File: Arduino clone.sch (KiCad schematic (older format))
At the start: 13 parts, among them U1 24LC1025, U2 24LC1025, U3 DS1337_AM, U4 ATMEGA328P-AU, Y1 Crystal, Y2 Crystal

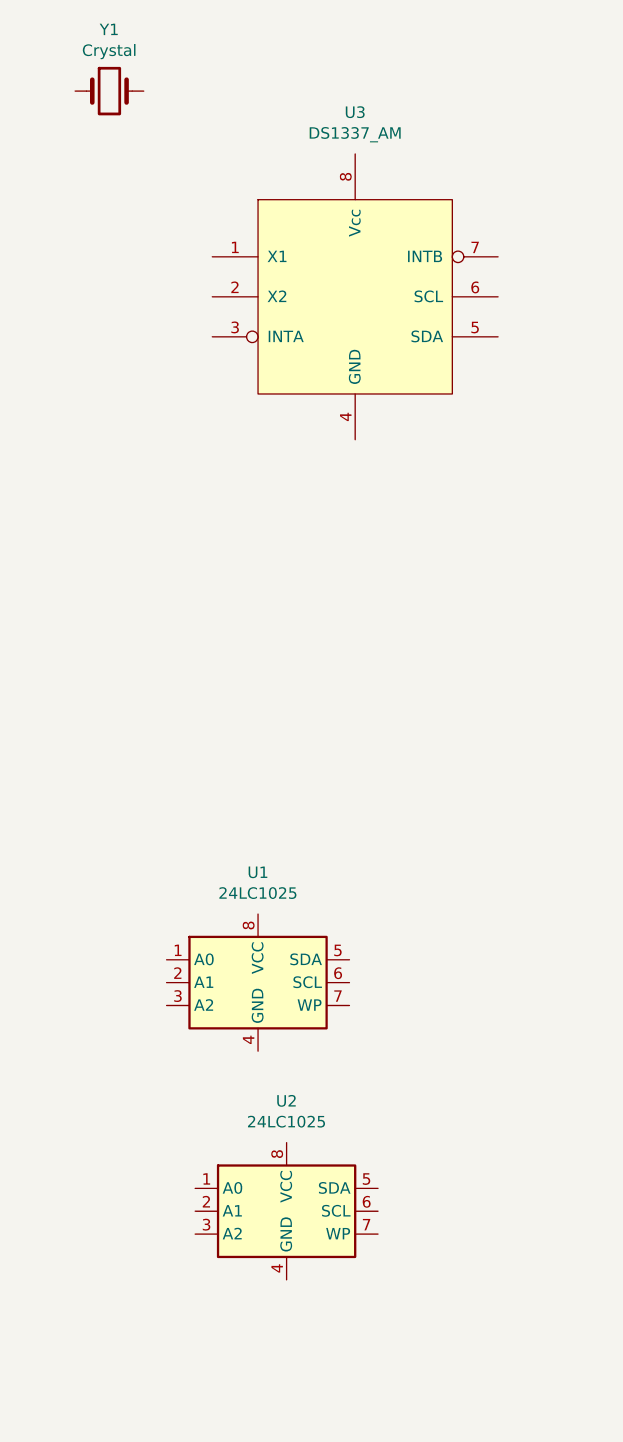
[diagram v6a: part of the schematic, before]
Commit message: Assigned footprints to symbols
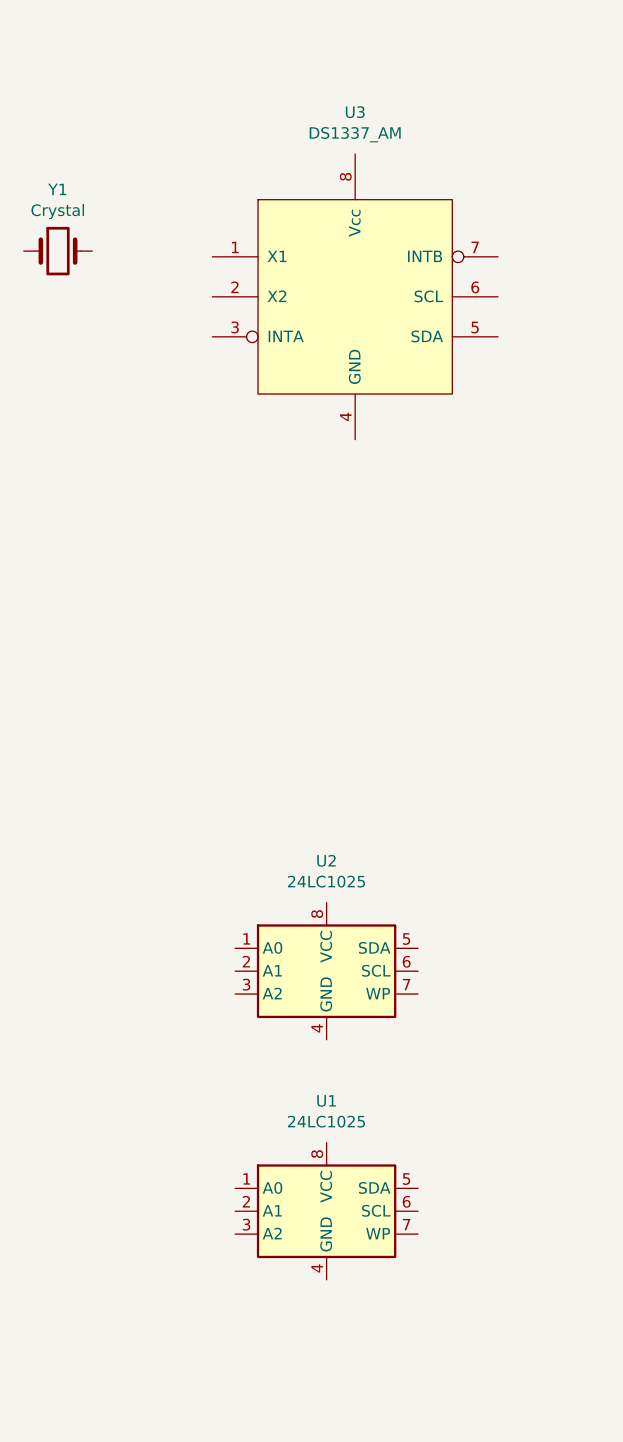
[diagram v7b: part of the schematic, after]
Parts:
- BT1: footprint (none) -> Connector_PinHeader_2.54mm:PinHeader_1x02_P2.54mm_Vertical
- C1, C2, C3: footprint (none) -> Capacitor_SMD:C_0805_2012Metric_Pad1.18x1.45mm_HandSolder
- D1: footprint (none) -> LED_SMD:LED_0805_2012Metric_Pad1.15x1.40mm_HandSolder
- R1, R2: footprint (none) -> Resistor_SMD:R_0805_2012Metric_Pad1.20x1.40mm_HandSolder
- U1, U2: footprint (none) -> Package_SO:SOIJ-8_5.3x5.3mm_P1.27mm
- U3: footprint (none) -> Package_SO:SO-8_5.3x6.2mm_P1.27mm
- Y1: footprint (none) -> Crystal:Crystal_SMD_MicroCrystal_CC7V-T1A-2Pin_3.2x1.5mm_HandSoldering
- Y2: footprint (none) -> Crystal:Crystal_SMD_5032-2Pin_5.0x3.2mm_HandSoldering
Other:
- moved on the sheet: U1, U2, Y1
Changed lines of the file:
@@
 F 0 "BT1" H 9558 1546 50  0000 L CNN
 F 1 "Battery" H 9558 1455 50  0000 L CNN
-F 2 "" V 9450 1560 50  0001 C CNN
+F 2 "Connector_PinHeader_2.54mm:PinHeader_1x02_P2.54mm_Vertical" V 9450 1560 50  0001 C CNN
 F 3 "~" V 9450 1560 50  0001 C CNN
 	1    9450 1500
@@
 F 0 "C1" H 4815 2546 50  0000 L CNN
 F 1 "C" H 4815 2455 50  0000 L CNN
-F 2 "" H 4738 2350 50  0001 C CNN
+F 2 "Capacitor_SMD:C_0805_2012Metric_Pad1.18x1.45mm_HandSolder" H 4738 2350 50  0001 C CNN
 F 3 "~" H 4700 2500 50  0001 C CNN
 	1    4700 2500
@@
 F 0 "C2" H 4815 2996 50  0000 L CNN
 F 1 "C" H 4815 2905 50  0000 L CNN
-F 2 "" H 4738 2800 50  0001 C CNN
+F 2 "Capacitor_SMD:C_0805_2012Metric_Pad1.18x1.45mm_HandSolder" H 4738 2800 50  0001 C CNN
 F 3 "~" H 4700 2950 50  0001 C CNN
 	1    4700 2950
@@
 F 0 "C3" H 9718 2196 50  0000 L CNN
 F 1 "CP" H 9718 2105 50  0000 L CNN
-F 2 "" H 9638 2000 50  0001 C CNN
+F 2 "Capacitor_SMD:C_0805_2012Metric_Pad1.18x1.45mm_HandSolder" H 9638 2000 50  0001 C CNN
 F 3 "~" H 9600 2150 50  0001 C CNN
 	1    9600 2150
@@
 F 0 "R1" H 5193 3771 50  0000 L CNN
 F 1 "R_US" H 5193 3680 50  0000 L CNN
-F 2 "" V 5165 3715 50  0001 C CNN
+F 2 "Resistor_SMD:R_0805_2012Metric_Pad1.20x1.40mm_HandSolder" V 5165 3715 50  0001 C CNN
 F 3 "~" H 5125 3725 50  0001 C CNN
 	1    5125 3725
@@
 F 0 "R2" H 5543 4696 50  0000 L CNN
 F 1 "R_US" H 5543 4605 50  0000 L CNN
-F 2 "" V 5515 4640 50  0001 C CNN
+F 2 "Resistor_SMD:R_0805_2012Metric_Pad1.20x1.40mm_HandSolder" V 5515 4640 50  0001 C CNN
 F 3 "~" H 5475 4650 50  0001 C CNN
 	1    5475 4650
@@
 L Device:Crystal Y1
 U 1 1 601C298C
-P 1450 1550
-F 0 "Y1" H 1450 1818 50  0000 C CNN
-F 1 "Crystal" H 1450 1727 50  0000 C CNN
-F 2 "" H 1450 1550 50  0001 C CNN
-F 3 "~" H 1450 1550 50  0001 C CNN
-	1    1450 1550
+P 1225 2250
+F 0 "Y1" H 1225 2518 50  0000 C CNN
+F 1 "Crystal" H 1225 2427 50  0000 C CNN
+F 2 "Crystal:Crystal_SMD_MicroCrystal_CC7V-T1A-2Pin_3.2x1.5mm_HandSoldering" H 1225 2250 50  0001 C CNN
+F 3 "~" H 1225 2250 50  0001 C CNN
+	1    1225 2250
 	1    0    0    -1
 $EndComp
@@
 F 0 "Y2" V 5154 2656 50  0000 L CNN
 F 1 "Crystal" V 5245 2656 50  0000 L CNN
-F 2 "" H 5200 2525 50  0001 C CNN
+F 2 "Crystal:Crystal_SMD_5032-2Pin_5.0x3.2mm_HandSoldering" H 5200 2525 50  0001 C CNN
 F 3 "~" H 5200 2525 50  0001 C CNN
 	1    5200 2525
@@
 L Memory_EEPROM:24LC1025 U2
 U 1 1 601CAEF5
-P 2225 6450
-F 0 "U2" H 2225 6931 50  0000 C CNN
-F 1 "24LC1025" H 2225 6840 50  0000 C CNN
-F 2 "" H 2225 6450 50  0001 C CNN
-F 3 "http://ww1.microchip.com/downloads/en/DeviceDoc/21941B.pdf" H 2225 6450 50  0001 C CNN
-	1    2225 6450
+P 2400 5400
+F 0 "U2" H 2400 5881 50  0000 C CNN
+F 1 "24LC1025" H 2400 5790 50  0000 C CNN
+F 2 "Package_SO:SOIJ-8_5.3x5.3mm_P1.27mm" H 2400 5400 50  0001 C CNN
+F 3 "http://ww1.microchip.com/downloads/en/DeviceDoc/21941B.pdf" H 2400 5400 50  0001 C CNN
+	1    2400 5400
 	1    0    0    -1
 $EndComp
@@
 F 0 "U3" H 2525 3256 50  0000 C CNN
 F 1 "DS1337_AM" H 2525 3165 50  0000 C CNN
-F 2 "" H 2525 2450 50  0001 C CNN
+F 2 "Package_SO:SO-8_5.3x6.2mm_P1.27mm" H 2525 2450 50  0001 C CNN
 F 3 "" H 2525 2450 50  0001 C CNN
 	1    2525 2450
@@
 L Memory_EEPROM:24LC1025 U1
 U 1 1 601B7371
-P 2100 5450
-F 0 "U1" H 2100 5931 50  0000 C CNN
-F 1 "24LC1025" H 2100 5840 50  0000 C CNN
-F 2 "" H 2100 5450 50  0001 C CNN
-F 3 "http://ww1.microchip.com/downloads/en/DeviceDoc/21941B.pdf" H 2100 5450 50  0001 C CNN
-	1    2100 5450
+P 2400 6450
+F 0 "U1" H 2400 6931 50  0000 C CNN
+F 1 "24LC1025" H 2400 6840 50  0000 C CNN
+F 2 "Package_SO:SOIJ-8_5.3x5.3mm_P1.27mm" H 2400 6450 50  0001 C CNN
+F 3 "http://ww1.microchip.com/downloads/en/DeviceDoc/21941B.pdf" H 2400 6450 50  0001 C CNN
+	1    2400 6450
 	1    0    0    -1
 $EndComp
@@
 F 0 "D1" H 5593 3667 50  0000 C CNN
 F 1 "LED" H 5593 3576 50  0000 C CNN
-F 2 "" H 5600 3450 50  0001 C CNN
+F 2 "LED_SMD:LED_0805_2012Metric_Pad1.15x1.40mm_HandSolder" H 5600 3450 50  0001 C CNN
 F 3 "~" H 5600 3450 50  0001 C CNN
 	1    5600 3450

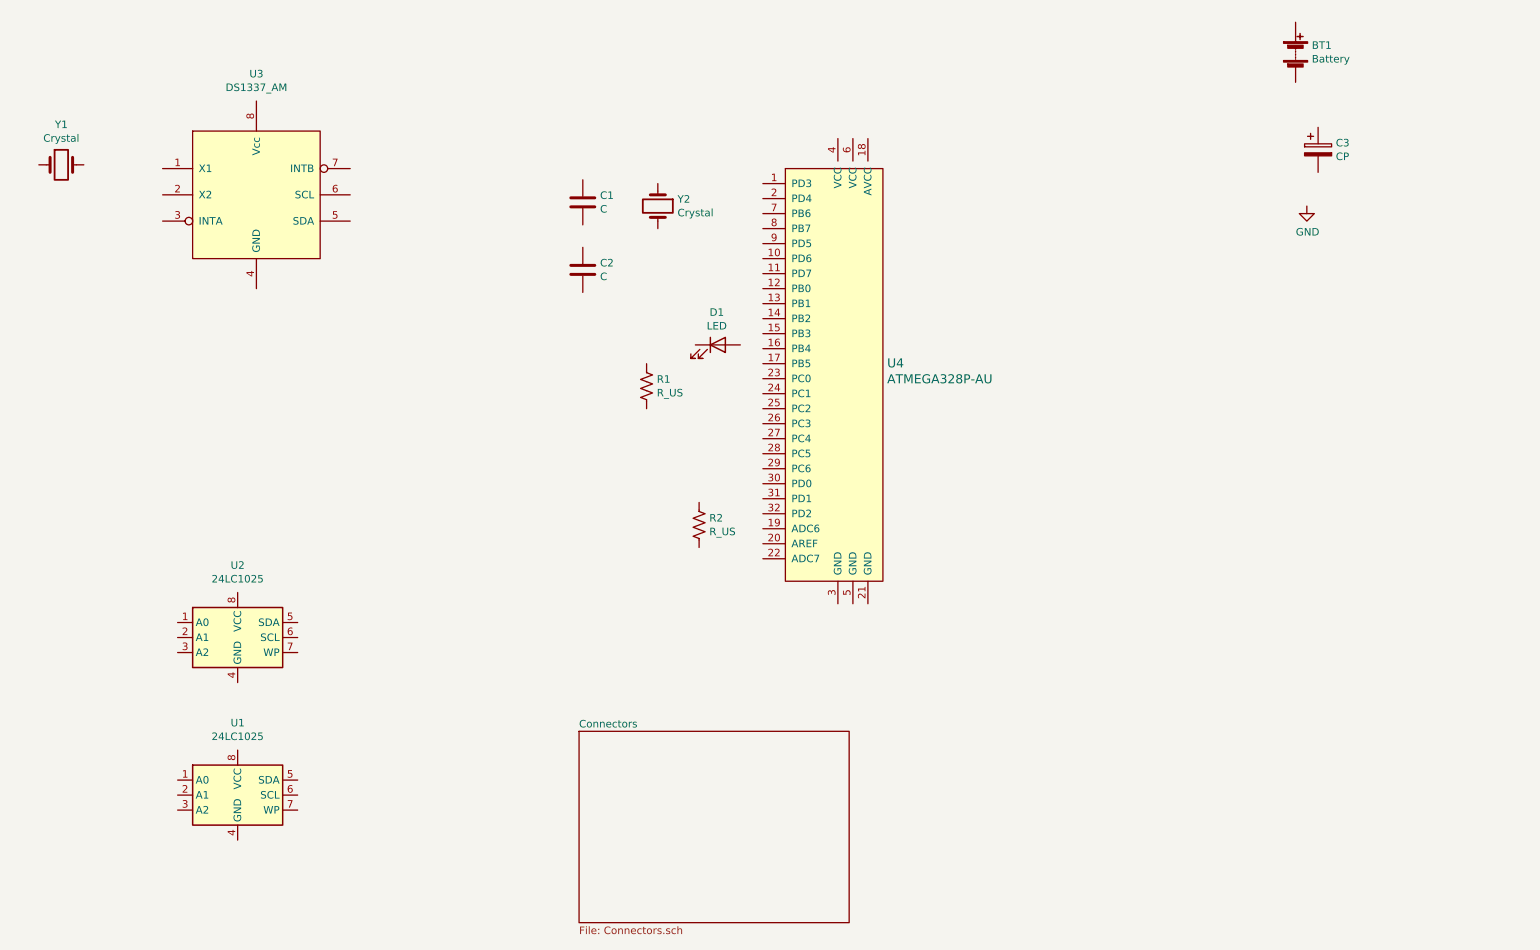
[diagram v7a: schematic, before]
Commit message: Added component values
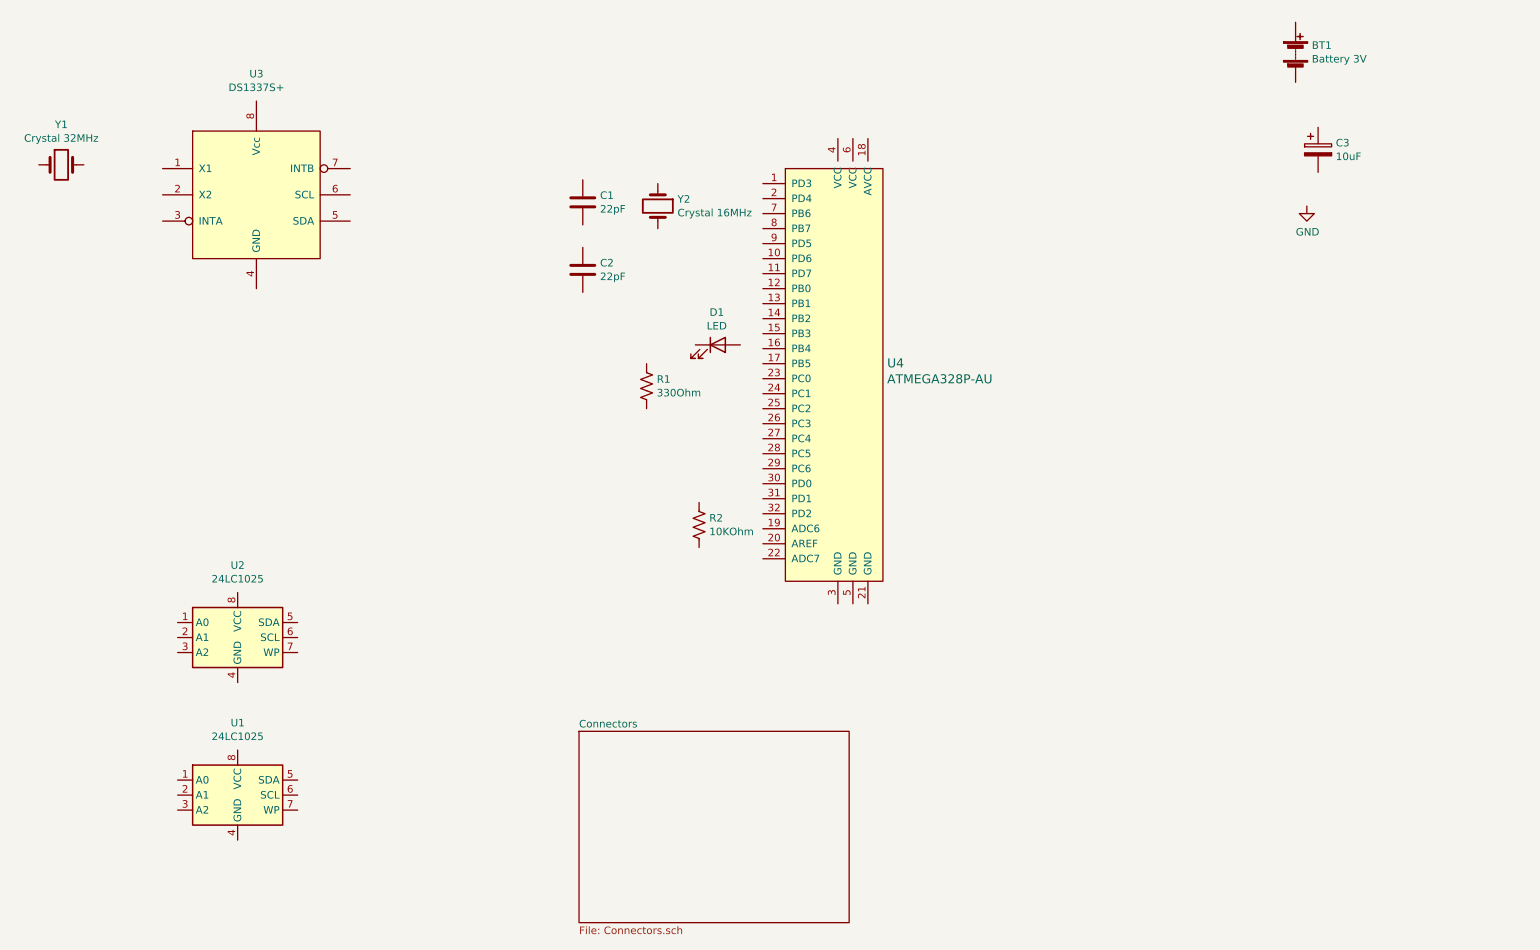
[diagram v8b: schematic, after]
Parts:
- BT1: value Battery -> Battery 3V
- C1, C2: value C -> 22pF
- C3: value CP -> 10uF
- R1: value R_US -> 330Ohm
- R2: value R_US -> 10KOhm
- U3: value DS1337_AM -> DS1337S+
- Y1: value Crystal -> Crystal 32MHz
- Y2: value Crystal -> Crystal 16MHz
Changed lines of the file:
@@
 P 9450 1500
 F 0 "BT1" H 9558 1546 50  0000 L CNN
-F 1 "Battery" H 9558 1455 50  0000 L CNN
+F 1 "Battery 3V" H 9558 1455 50  0000 L CNN
 F 2 "Connector_PinHeader_2.54mm:PinHeader_1x02_P2.54mm_Vertical" V 9450 1560 50  0001 C CNN
 F 3 "~" V 9450 1560 50  0001 C CNN
@@
 P 4700 2500
 F 0 "C1" H 4815 2546 50  0000 L CNN
-F 1 "C" H 4815 2455 50  0000 L CNN
+F 1 "22pF" H 4815 2455 50  0000 L CNN
 F 2 "Capacitor_SMD:C_0805_2012Metric_Pad1.18x1.45mm_HandSolder" H 4738 2350 50  0001 C CNN
 F 3 "~" H 4700 2500 50  0001 C CNN
@@
 P 4700 2950
 F 0 "C2" H 4815 2996 50  0000 L CNN
-F 1 "C" H 4815 2905 50  0000 L CNN
+F 1 "22pF" H 4815 2905 50  0000 L CNN
 F 2 "Capacitor_SMD:C_0805_2012Metric_Pad1.18x1.45mm_HandSolder" H 4738 2800 50  0001 C CNN
 F 3 "~" H 4700 2950 50  0001 C CNN
@@
 P 9600 2150
 F 0 "C3" H 9718 2196 50  0000 L CNN
-F 1 "CP" H 9718 2105 50  0000 L CNN
+F 1 "10uF" H 9718 2105 50  0000 L CNN
 F 2 "Capacitor_SMD:C_0805_2012Metric_Pad1.18x1.45mm_HandSolder" H 9638 2000 50  0001 C CNN
 F 3 "~" H 9600 2150 50  0001 C CNN
@@
 P 5125 3725
 F 0 "R1" H 5193 3771 50  0000 L CNN
-F 1 "R_US" H 5193 3680 50  0000 L CNN
+F 1 "330Ohm" H 5193 3680 50  0000 L CNN
 F 2 "Resistor_SMD:R_0805_2012Metric_Pad1.20x1.40mm_HandSolder" V 5165 3715 50  0001 C CNN
 F 3 "~" H 5125 3725 50  0001 C CNN
@@
 P 5475 4650
 F 0 "R2" H 5543 4696 50  0000 L CNN
-F 1 "R_US" H 5543 4605 50  0000 L CNN
+F 1 "10KOhm" H 5543 4605 50  0000 L CNN
 F 2 "Resistor_SMD:R_0805_2012Metric_Pad1.20x1.40mm_HandSolder" V 5515 4640 50  0001 C CNN
 F 3 "~" H 5475 4650 50  0001 C CNN
@@
 P 1225 2250
 F 0 "Y1" H 1225 2518 50  0000 C CNN
-F 1 "Crystal" H 1225 2427 50  0000 C CNN
+F 1 "Crystal 32MHz" H 1225 2427 50  0000 C CNN
 F 2 "Crystal:Crystal_SMD_MicroCrystal_CC7V-T1A-2Pin_3.2x1.5mm_HandSoldering" H 1225 2250 50  0001 C CNN
 F 3 "~" H 1225 2250 50  0001 C CNN
@@
 P 5200 2525
 F 0 "Y2" V 5154 2656 50  0000 L CNN
-F 1 "Crystal" V 5245 2656 50  0000 L CNN
+F 1 "Crystal 16MHz" V 5245 2656 50  0000 L CNN
 F 2 "Crystal:Crystal_SMD_5032-2Pin_5.0x3.2mm_HandSoldering" H 5200 2525 50  0001 C CNN
 F 3 "~" H 5200 2525 50  0001 C CNN
@@
 P 2525 2450
 F 0 "U3" H 2525 3256 50  0000 C CNN
-F 1 "DS1337_AM" H 2525 3165 50  0000 C CNN
+F 1 "DS1337S+" H 2525 3165 50  0000 C CNN
 F 2 "Package_SO:SO-8_5.3x6.2mm_P1.27mm" H 2525 2450 50  0001 C CNN
 F 3 "" H 2525 2450 50  0001 C CNN
